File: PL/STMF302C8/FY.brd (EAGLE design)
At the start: 70 x 69 mm, 55 parts, among them J1 CON-SD-CARD_MICROSD-2908-05, J2 Flash Programming, U1 AS72652-BLGT, U2 AS72653-BLGT, U3 STM32F302C8T6, U4 AS72651-BLGT, U5 AMS1117-3.3, U6 4MB Flash, X1 JST-XH-04-PIN-LONG-PAD, Y2 ABM2B-8.000MHZ-10-1-U-T

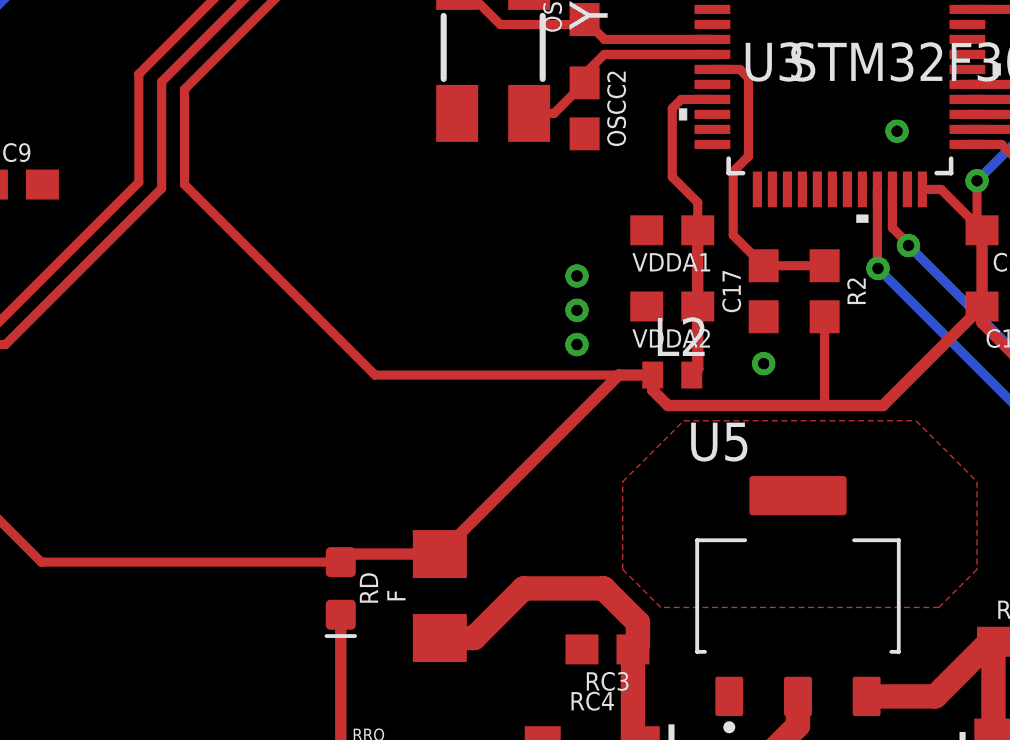
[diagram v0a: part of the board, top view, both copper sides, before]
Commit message: packages was modified according to stock situation
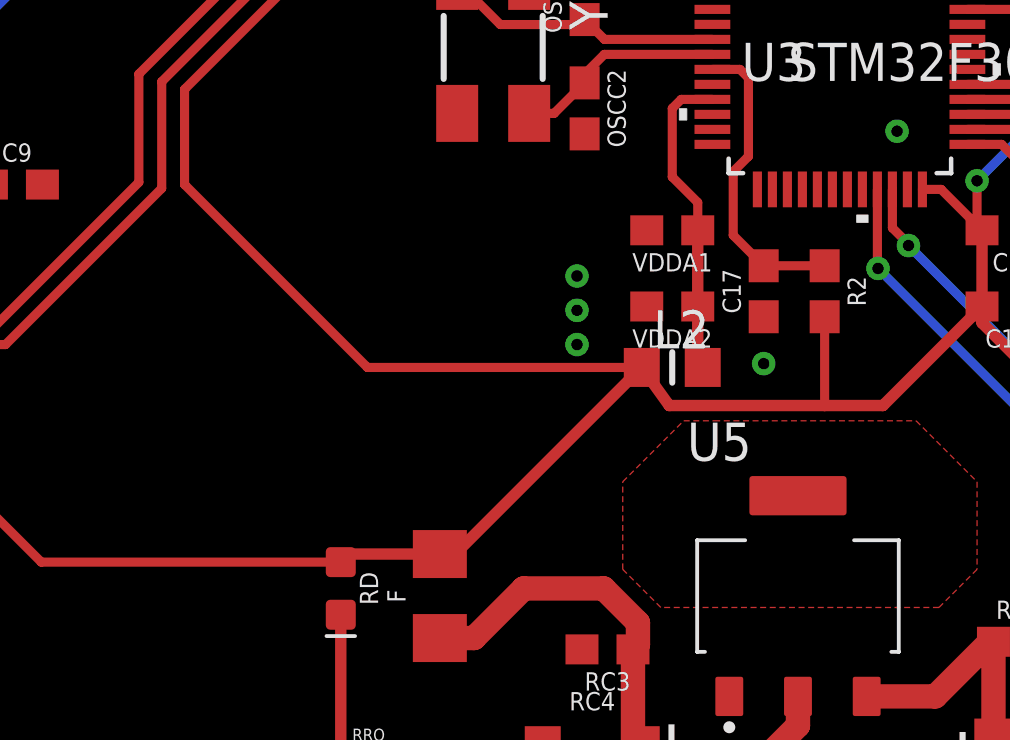
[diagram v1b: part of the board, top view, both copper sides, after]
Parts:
- L2: value BLM15HB221SN1 -> (none); device inductors:0402 -> 52101-101-REV-A_v16:RC-MASTER-SMD_L0805MP
- moved L2 0.25 mm to (32.6, 24.5)
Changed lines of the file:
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@@
 <attribute name="VALUE" x="50.673" y="33.401" size="0.6096" layer="27" font="vector" ratio="20" rot="R90"/>
 </element>
-<element name="L2" library="inductors" library_urn="urn:adsk.eagle:library:243" package="0402" package3d_urn="urn:adsk.eagle:package:15132/1" value="BLM15HB221SN1" x="32.639" y="24.257" smashed="yes">
-<attribute name="NAME" x="32.004" y="24.892" size="1.27" layer="25"/>
-<attribute name="ORDER_URL" value="https://eu.mouser.com/ProductDetail/Murata-Electronics/NFZ15SR152SN10D?qs=rkhjVJ6%2F3EK7NITaH%252B9%252Bxg%3D%3D" x="60.579" y="-30.353" size="1.778" layer="27" display="off"/>
-<attribute name="POPULARITY" value="0" x="60.579" y="-30.353" size="1.778" layer="27" display="off"/>
-<attribute name="VALUE" x="32.004" y="22.352" size="1.27" layer="27"/>
+<element name="L2" library="52101-101-REV-A_v16" library_urn="urn:adsk.eagle:library:21899384" package="RC-MASTER-SMD_L0805MP" package3d_urn="urn:adsk.eagle:package:15662270/2" value="" x="32.639" y="24.511" smashed="yes">
+<attribute name="NAME" x="32.004" y="25.146" size="1.27" layer="25"/>
+<attribute name="ORDER_URL" value="https://eu.mouser.com/ProductDetail/Murata-Electronics/NFZ15SR152SN10D?qs=rkhjVJ6%2F3EK7NITaH%252B9%252Bxg%3D%3D" x="60.579" y="-30.099" size="1.778" layer="27" display="off"/>
+<attribute name="VALUE" x="32.004" y="22.606" size="1.27" layer="27"/>
 </element>
 <element name="OSCC1" library="SparkFun-Capacitors" library_urn="urn:adsk.eagle:library:510" package="0603" package3d_urn="urn:adsk.eagle:package:37414/1" value="25pF" x="29.718" y="36.957" smashed="yes" rot="R90">
@@
 <wire x1="24.892" y1="18.291" x2="21.859" y2="18.291" width="0.381" layer="1"/>
 <wire x1="21.859" y1="18.291" x2="21.59" y2="18.022" width="0.381" layer="1"/>
-<wire x1="31.989" y1="24.257" x2="30.858" y2="24.257" width="0.381" layer="1"/>
-<wire x1="30.858" y1="24.257" x2="24.892" y2="18.291" width="0.381" layer="1"/>
+<wire x1="31.623" y1="24.511" x2="31.62" y2="24.511" width="0.381" layer="1"/>
+<wire x1="31.62" y1="24.511" x2="25.4" y2="18.291" width="0.381" layer="1"/>
+<wire x1="25.4" y1="18.291" x2="24.892" y2="18.291" width="0.381" layer="1"/>
 <wire x1="42.965" y1="29.083" x2="42.965" y2="28.829" width="0.381" layer="1"/>
 <wire x1="42.965" y1="28.829" x2="42.965" y2="26.543" width="0.381" layer="1"/>
@@
 <wire x1="67.056" y1="49.149" x2="67.056" y2="34.925" width="0.3048" layer="1"/>
 <wire x1="67.056" y1="34.925" x2="65.952" y2="33.821" width="0.3048" layer="1"/>
-<wire x1="31.989" y1="24.257" x2="22.733" y2="24.257" width="0.3048" layer="1"/>
-<wire x1="22.733" y1="24.257" x2="16.383" y2="30.607" width="0.3048" layer="1"/>
+<wire x1="31.623" y1="24.511" x2="22.479" y2="24.511" width="0.3048" layer="1"/>
+<wire x1="22.479" y1="24.511" x2="16.383" y2="30.607" width="0.3048" layer="1"/>
 <wire x1="16.383" y1="30.607" x2="16.383" y2="33.782" width="0.3048" layer="1"/>
 <wire x1="16.383" y1="33.782" x2="24.765" y2="42.164" width="0.3048" layer="1"/>
@@
 <wire x1="42.457" y1="66.167" x2="42.457" y2="63.881" width="0.3048" layer="1"/>
 <wire x1="26.201" y1="64.516" x2="19.939" y2="64.516" width="0.3048" layer="1"/>
-<wire x1="32.497" y1="23.241" x2="31.989" y2="23.749" width="0.381" layer="1"/>
-<wire x1="31.989" y1="24.257" x2="31.989" y2="23.749" width="0.381" layer="1"/>
-<wire x1="32.497" y1="23.241" x2="37.719" y2="23.241" width="0.381" layer="1"/>
+<wire x1="31.623" y1="24.511" x2="32.538" y2="23.241" width="0.381" layer="1"/>
+<wire x1="32.538" y1="23.241" x2="37.719" y2="23.241" width="0.381" layer="1"/>
 <contactref element="X1" pad="4"/>
 <wire x1="42.965" y1="26.543" x2="42.965" y2="25.996" width="0.381" layer="1"/>
@@
 <contactref element="VDDA2" pad="1"/>
 <contactref element="VDDA1" pad="1"/>
-<wire x1="33.289" y1="24.257" x2="33.489" y2="24.457" width="0.381" layer="1"/>
-<wire x1="33.489" y1="24.457" x2="33.489" y2="26.543" width="0.381" layer="1"/>
+<wire x1="33.655" y1="24.511" x2="33.489" y2="24.711" width="0.381" layer="1"/>
+<wire x1="33.489" y1="24.711" x2="33.489" y2="26.543" width="0.381" layer="1"/>
 <wire x1="33.489" y1="26.543" x2="33.489" y2="29.083" width="0.381" layer="1"/>
 <wire x1="32.639" y1="30.861" x2="32.639" y2="33.147" width="0.3048" layer="1"/>
